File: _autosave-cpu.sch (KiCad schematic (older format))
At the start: 16 parts, among them J1 Conn_02x05_Odd_Even, SW2 SW_Push, SW3 SW_Push, U1 E73-2G4M04S-52832

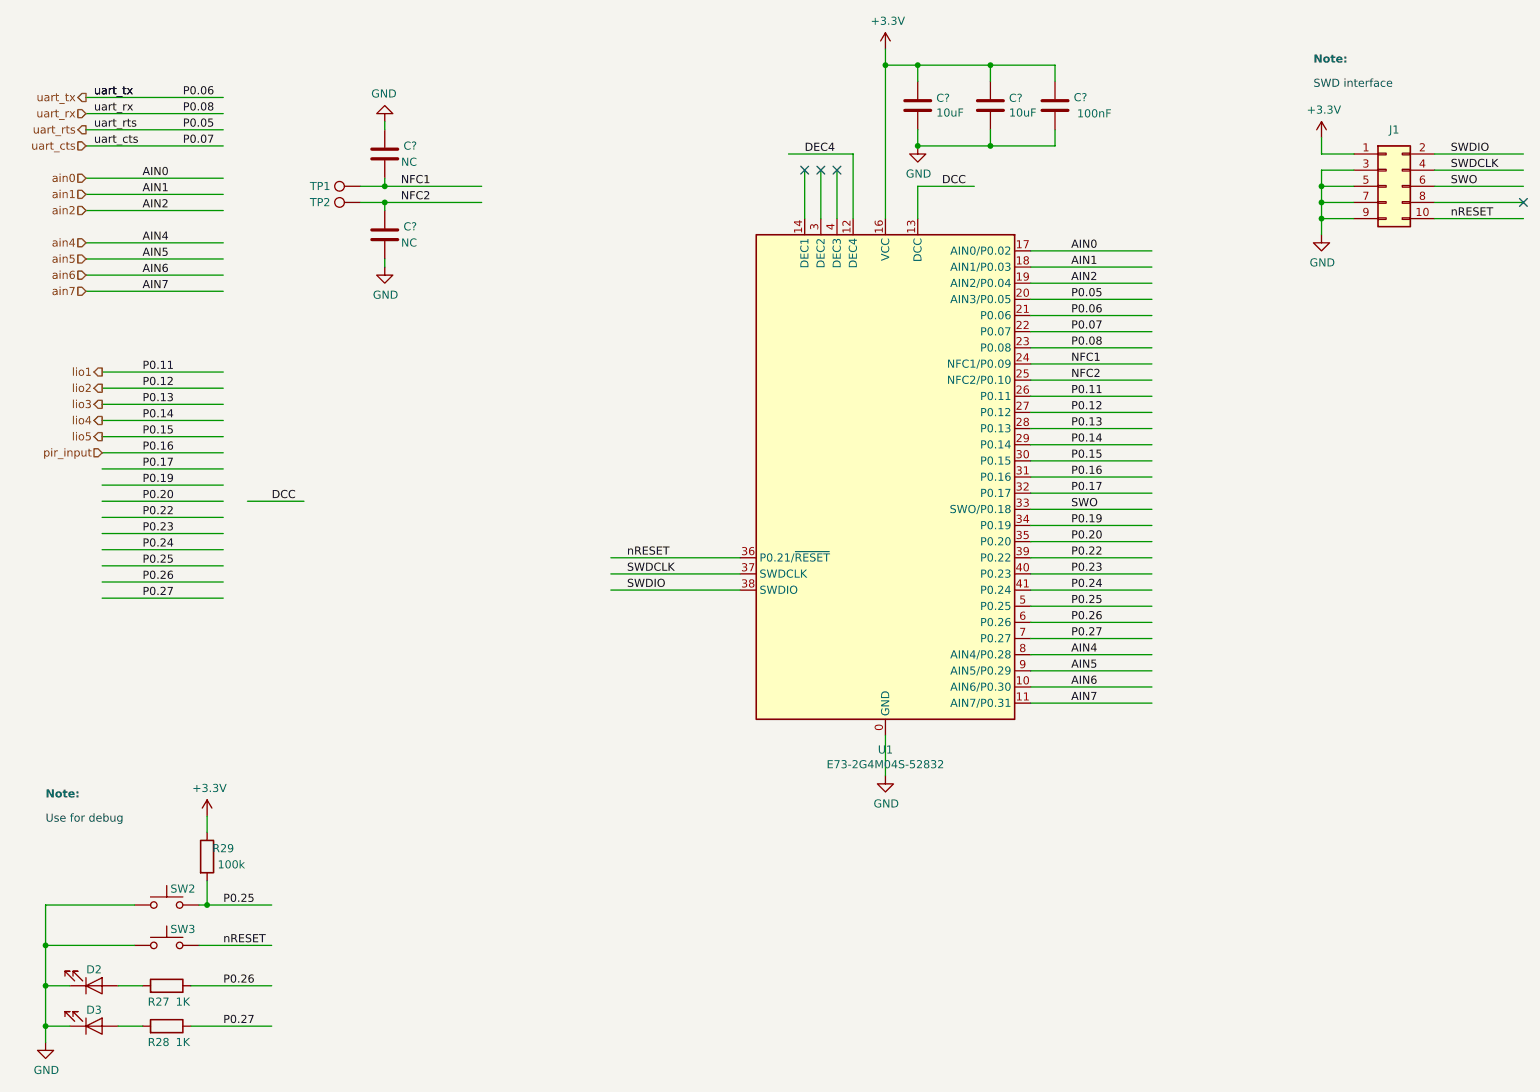
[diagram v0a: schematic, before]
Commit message: more layout + resized pcb to 100 x 80
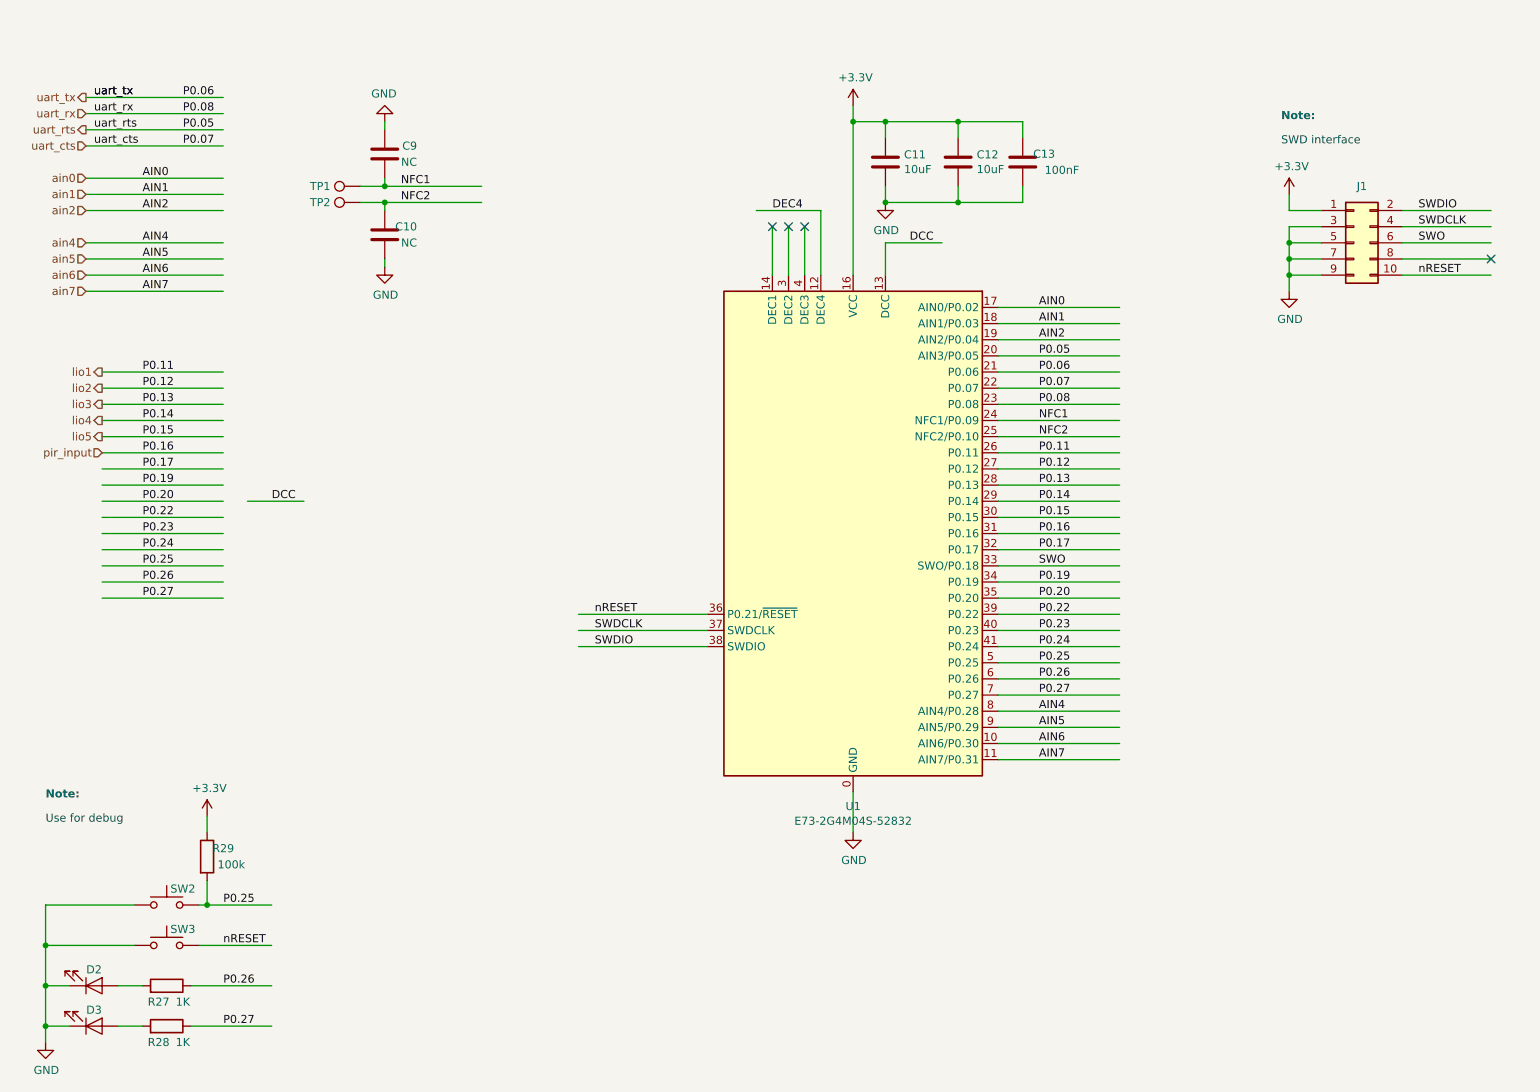
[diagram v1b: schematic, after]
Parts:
- gave numbers to parts that had none: 5
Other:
- moved on the sheet: C11, C12, C13, J1, U1
